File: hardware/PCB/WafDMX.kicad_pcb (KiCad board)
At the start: 2 copper layers, 91.4 x 101.6 mm, 54 parts, among them J1 Wuerth_7499010121A, J2 Screw_Terminal_01x02, J3 USB_B_Micro, J4 Conn_01x04_Female, Q1 MMDT2222A, U1 AMS1117-3.3, U2 LAN8720A, U3 CH340C, U4 ESP32-WROOM-32D, U5 MAX3485, X1 ASV-50MHz

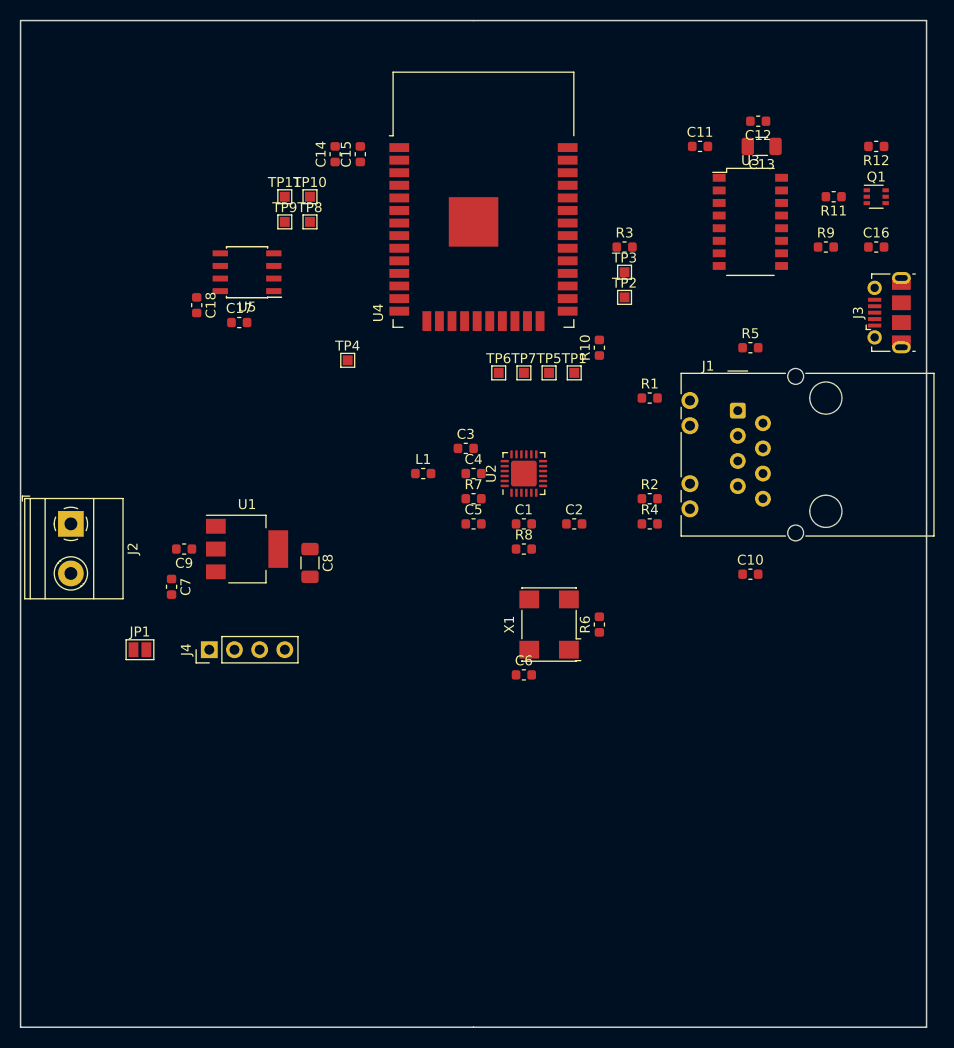
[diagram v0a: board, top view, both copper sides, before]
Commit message: Change Testpoints to TH, start placing
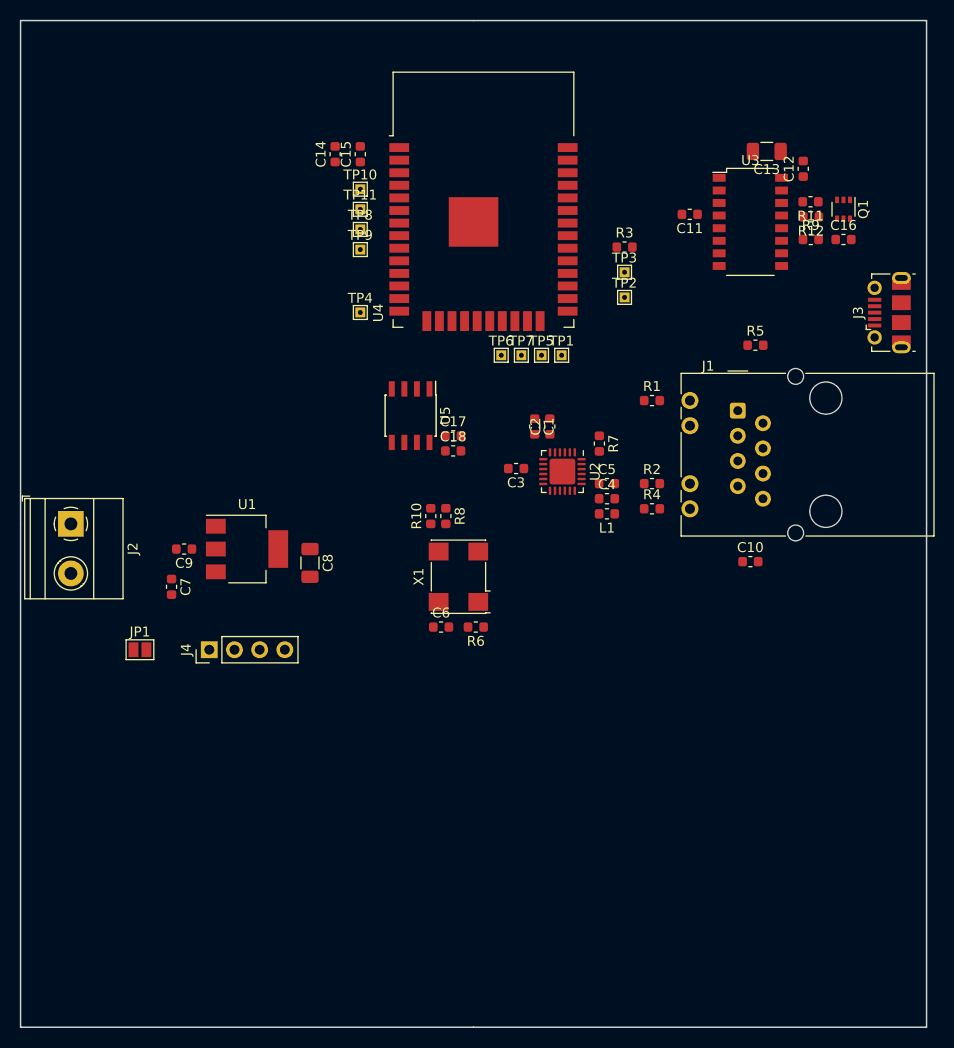
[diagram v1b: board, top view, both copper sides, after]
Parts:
- TP1, TP10, TP11, TP2, TP3, TP4, TP5, TP6, TP7, TP8, TP9: footprint TestPoint:TestPoint_Pad_1.0x1.0mm -> TestPoint:TestPoint_THTPad_1.0x1.0mm_Drill0.5mm
- moved C18 29.8 mm to (145.3, 94.2), turned to 0 degrees
- moved C17 24.4 mm to (145.3, 92.7)
- moved R10 24.0 mm to (143.0, 100.8)
- moved U5 22.0 mm to (141.0, 90.7), turned to 270 degrees
- moved L1 19.0 mm to (160.8, 100.6), turned to 180 degrees
- moved C5 14.1 mm to (160.8, 97.5)
- moved R7 13.9 mm to (160.0, 93.5), turned to 270 degrees
- moved C4 13.7 mm to (160.8, 99.1)
- moved R6 12.5 mm to (147.5, 112.0), turned to 180 degrees
- moved X1 10.3 mm to (145.8, 106.9)
- moved C2 10.1 mm to (155.0, 91.8), turned to 90 degrees
- moved C1 9.89 mm to (153.5, 91.8), turned to 270 degrees
- moved R12 9.69 mm to (181.4, 70.6)
- moved C6 9.65 mm to (144.0, 112.0)
- moved R8 8.55 mm to (144.5, 100.8), turned to 270 degrees
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
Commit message: First routing of PCB
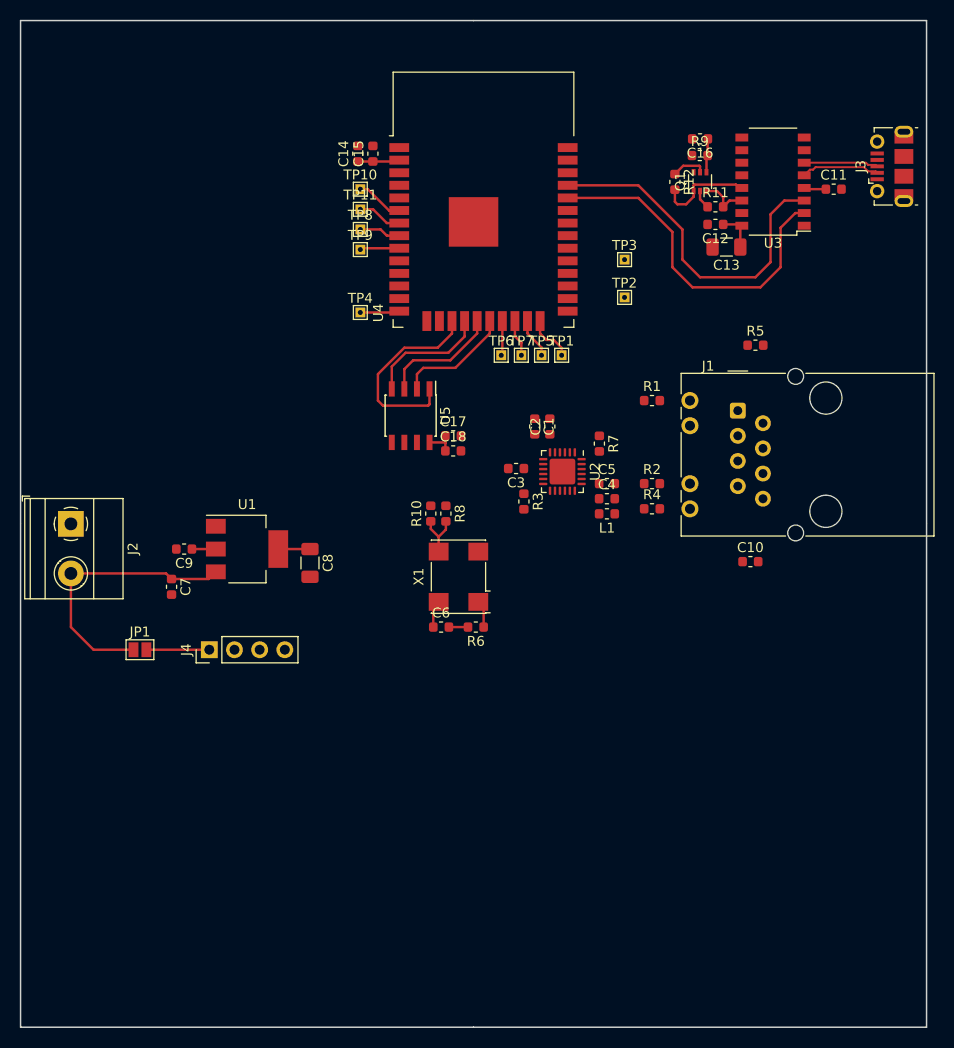
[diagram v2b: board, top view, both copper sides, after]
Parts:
- moved R3 27.6 mm to (152.4, 99.3), turned to 270 degrees
- moved C16 17.7 mm to (170.2, 62.7), turned to 180 degrees
- moved J3 14.8 mm to (189.5, 65.5)
- moved C11 14.7 mm to (183.7, 67.8), turned to 0 degrees
- moved Q1 14.7 mm to (170.2, 67.1), turned to 90 degrees
- moved R12 14.2 mm to (167.6, 67.1), turned to 270 degrees
- moved R9 14.0 mm to (170.2, 64.4)
- moved C12 10.5 mm to (171.7, 71.4), turned to 180 degrees
- moved C13 10.5 mm to (172.8, 73.7)
- moved R11 9.61 mm to (171.7, 69.6), turned to 0 degrees
- moved U3 4.66 mm to (177.5, 67.1), turned to 180 degrees
- moved C14 2.29 mm to (135.6, 64.2)
- moved C15 1.27 mm to (137.2, 64.2)
- moved TP3 1.27 mm to (162.6, 74.9)
- moved R10 0.25 mm to (143.0, 100.6)
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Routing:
- net /ESP32_TX: track 0.00 -> 35.5 mm
- net /ESP32_RX: track 0.00 -> 35.1 mm
- net VCC: track 0.00 -> 27.8 mm
- net /DMX_MAX_OUT: track 0.00 -> 20.1 mm
- net +3V3: track 0.00 -> 20.0 mm
- net /DMX_MAX_IN: track 0.00 -> 12.4 mm
- net /DMX_DE: track 0.00 -> 12.1 mm
- net /DMX_RE: track 0.00 -> 11.8 mm
- net /DTR: track 0.00 -> 9.72 mm
- net /USB_DN: track 0.00 -> 7.93 mm
- net /USB_DP: track 0.00 -> 7.51 mm
- net Net-(J4-Pad1): track 0.00 -> 6.35 mm
- net /PHY_CLK: track 0.00 -> 5.24 mm
- net /RTS: track 0.00 -> 5.05 mm
- net Net-(TP10-Pad1): track 0.00 -> 4.82 mm
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
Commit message: Add routing
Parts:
- added J5: XLR3, WafDMX:XLR_Neutrik_NC3FAAH_Horizontal, F.Cu at (117.5, 94.5)
- added J6: XLR3, WafDMX:XLR_Neutrik_NC3MAAH_Horizontal, F.Cu at (117.5, 120.6)
- J2: footprint TerminalBlock_Phoenix:TerminalBlock_Phoenix_MKDS-1,5-2_1x02_P5.00mm_Horizontal -> WafDMX:TerminalBlock_WAGO_2604-1102_2x05_P5.00mm_30Degree
- R3, R4: value 33R -> 10K
- moved J3 88.8 mm to (146.4, 143.2), turned to 0 degrees
- moved C11 75.3 mm to (143.4, 131.4), turned to 180 degrees
- moved U3 67.6 mm to (144.8, 126.2), turned to 90 degrees
- moved C13 59.1 mm to (138.2, 121.5), turned to 90 degrees
- moved R11 58.4 mm to (142.9, 120.4), turned to 270 degrees
- moved R12 58.3 mm to (145.9, 121.2), turned to 180 degrees
- moved C12 58.2 mm to (140.5, 120.4), turned to 90 degrees
- moved Q1 57.4 mm to (145.4, 118.9), turned to 0 degrees
- moved J1 55.8 mm to (121.8, 70.5), turned to 180 degrees
- moved C6 52.0 mm to (153.8, 61.0), turned to 180 degrees
- moved C16 51.9 mm to (130.3, 95.9), turned to 270 degrees
- moved C10 51.5 mm to (134.5, 73.9)
- moved R6 51.1 mm to (150.3, 61.0), turned to 0 degrees
- moved R2 49.0 mm to (130.5, 63.1), turned to 180 degrees
- moved R9 48.9 mm to (130.3, 92.7), turned to 270 degrees
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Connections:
- J3 pad 1: (no net) -> Net-(J3-Pad1)
- J3 pad 4: (no net) -> Net-(J3-Pad4)
- U2 pad 14: (no net) -> Net-(U2-Pad14)
- U2 pad 4: (no net) -> Net-(U2-Pad4)
- U3 pad 10: (no net) -> Net-(U3-Pad10)
- U3 pad 11: (no net) -> Net-(U3-Pad11)
- U3 pad 12: (no net) -> Net-(U3-Pad12)
- U3 pad 15: (no net) -> Net-(U3-Pad15)
- U3 pad 7: (no net) -> Net-(U3-Pad7)
- U3 pad 8: (no net) -> Net-(U3-Pad8)
- U3 pad 9: (no net) -> Net-(U3-Pad9)
- U4 pad 32: (no net) -> Net-(U4-Pad32)
- U4 pad 4: (no net) -> Net-(U4-Pad4)
- U4 pad 5: (no net) -> Net-(U4-Pad5)
- U5 pad 6: (no net) -> Net-(J5-Pad3)
- U5 pad 7: (no net) -> Net-(J5-Pad2)
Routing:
- net +3V3: track 20.0 -> 203.3 mm, vias 0 -> 10
- net Net-(J5-Pad3): track 0.00 -> 65.0 mm
- net /PHY_CLK_EN: track 2.76 -> 65.7 mm
- net /IO0: track 0.00 -> 62.8 mm
- net /PHY_POWER: track 0.00 -> 61.6 mm, vias 0 -> 2
- net /SMI_MDIO: track 0.00 -> 56.6 mm, vias 0 -> 2
- net /EMAC_TXD0: track 0.00 -> 54.9 mm
- net /EMAC_RX_DV: track 0.00 -> 54.4 mm, vias 0 -> 2
- net /PHY_TX_N: track 0.00 -> 53.8 mm
- net /EMAC_TX_EN: track 0.00 -> 52.5 mm
- net /EMAC_TXD1: track 0.00 -> 51.6 mm, vias 0 -> 2
- net /PHY_TX_P: track 0.00 -> 49.3 mm
- net /SPI_CLK: track 0.00 -> 48.4 mm
- net /EMAC_RXD1: track 0.00 -> 48.0 mm
- net /SPI_MOSI: track 0.00 -> 47.9 mm
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- added copper zone on B.Cu, net GND
- added copper zone on F.Cu, net GND
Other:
- board size 91.4 x 101.6 mm -> 61.8 x 90 mm

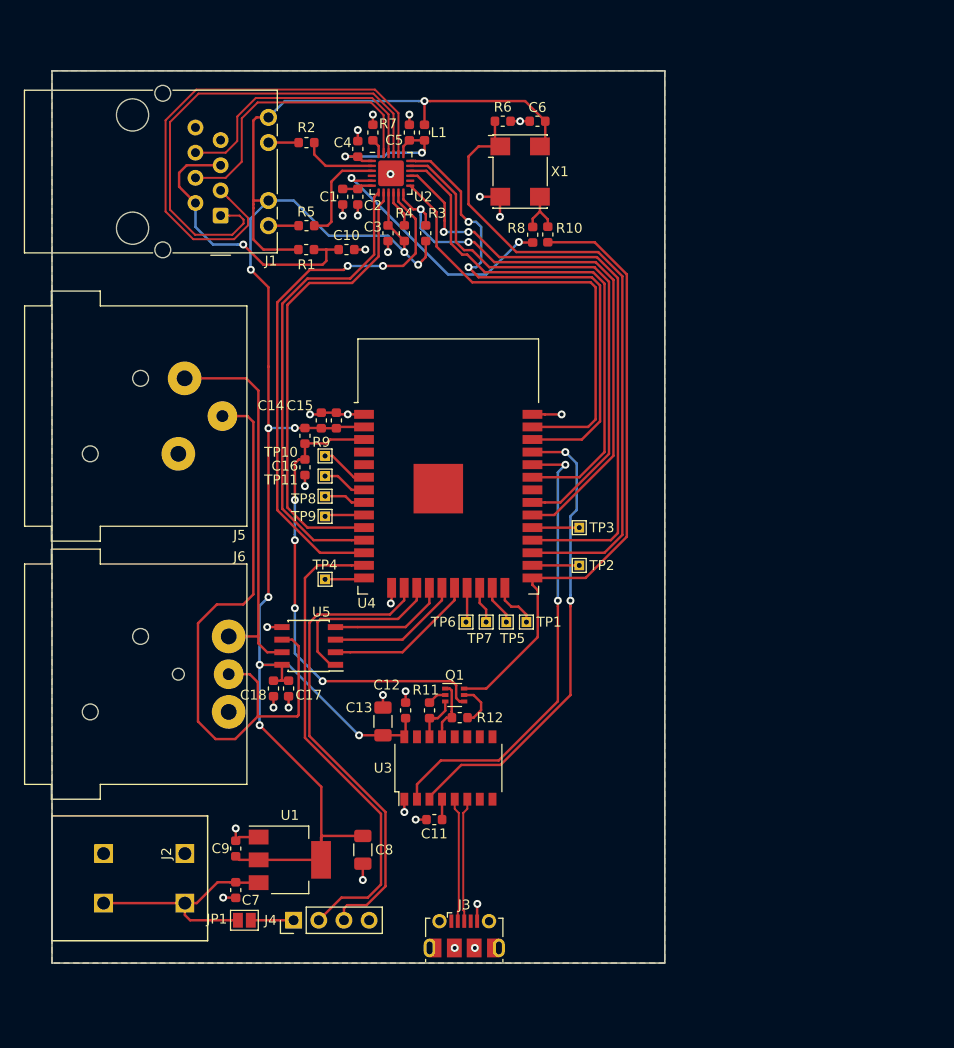
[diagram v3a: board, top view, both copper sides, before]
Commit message: Add 3V3-5V level shifter
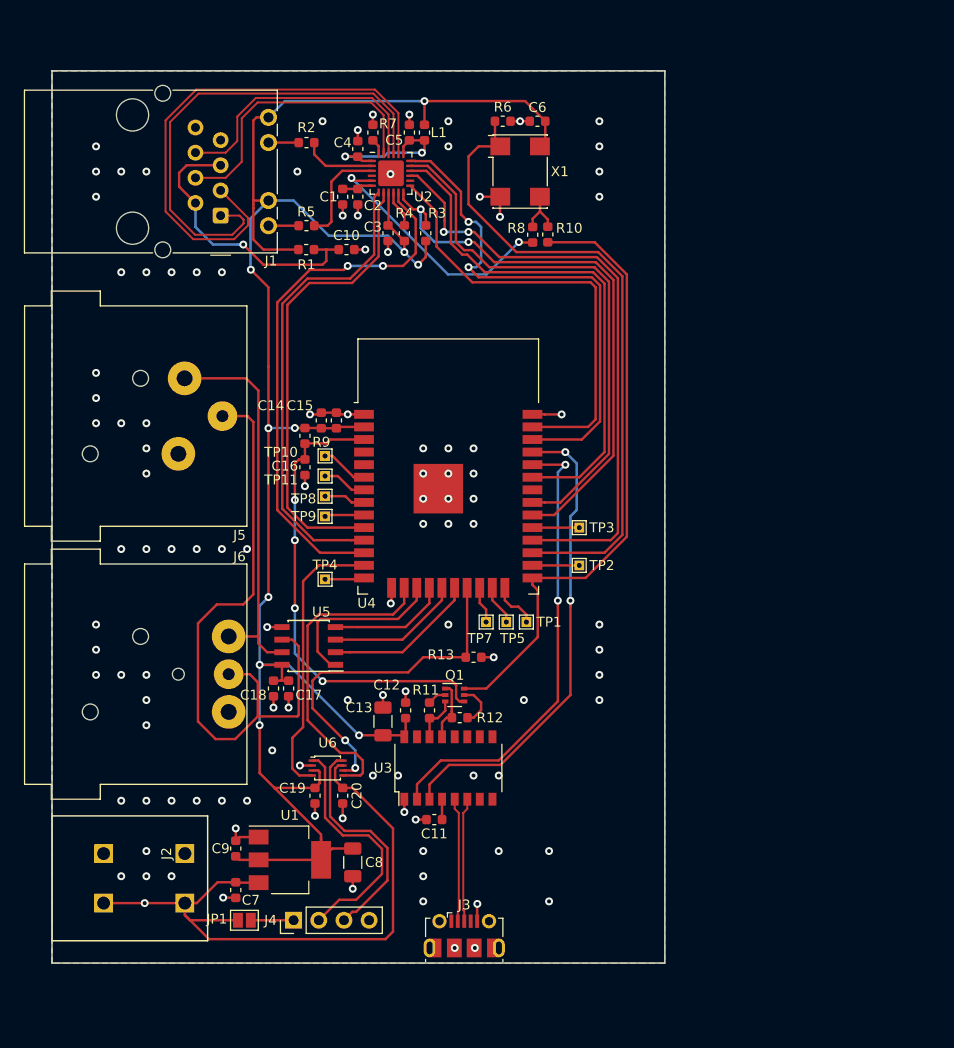
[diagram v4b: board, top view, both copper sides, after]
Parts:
- removed TP6: TestPoint, TestPoint:TestPoint_THTPad_1.0x1.0mm_Drill0.5mm
- added C19: 0.1 uF, Capacitor_SMD:C_0603_1608Metric, F.Cu at (131.3, 129.0)
- added C20: 0.1 uF, Capacitor_SMD:C_0603_1608Metric, F.Cu at (134.1, 129.0)
- added R13: R_Small, Resistor_SMD:R_0603_1608Metric, F.Cu at (147.3, 115.1)
- added U6: TXB0102DCU, Package_SO:VSSOP-8_2.4x2.1mm_P0.5mm, F.Cu at (132.6, 126.2)
- moved C8 1.63 mm to (135.1, 135.8)
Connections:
- J3 pad 1: Net-(J3-Pad1) -> (no net)
- J3 pad 4: Net-(J3-Pad4) -> (no net)
- J4 pad 2: /SPI_CLK -> /5V_SPI_CLK
- J4 pad 3: /SPI_MOSI -> /5V_SPI_MOSI
- U2 pad 14: Net-(U2-Pad14) -> (no net)
- U2 pad 4: Net-(U2-Pad4) -> (no net)
- U3 pad 10: Net-(U3-Pad10) -> (no net)
- U3 pad 11: Net-(U3-Pad11) -> (no net)
- U3 pad 12: Net-(U3-Pad12) -> (no net)
- U3 pad 15: Net-(U3-Pad15) -> (no net)
- U3 pad 7: Net-(U3-Pad7) -> (no net)
- U3 pad 8: Net-(U3-Pad8) -> (no net)
- U3 pad 9: Net-(U3-Pad9) -> (no net)
- U4 pad 21: Net-(TP6-Pad1) -> /SPI_OE
- U4 pad 32: Net-(U4-Pad32) -> (no net)
- U4 pad 4: Net-(U4-Pad4) -> (no net)
- U4 pad 5: Net-(U4-Pad5) -> (no net)
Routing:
- net VCC: track 23.3 -> 66.0 mm, vias 0 -> 1
- net /SPI_OE: track 0.00 -> 35.5 mm, vias 0 -> 2
- net /5V_SPI_CLK: track 0.00 -> 24.6 mm
- net /5V_SPI_MOSI: track 0.00 -> 23.0 mm
- net /SPI_CLK: track 48.4 -> 28.5 mm
- net /SPI_MOSI: track 47.9 -> 32.4 mm
- net +3V3: track 203.3 -> 209.4 mm
- net GND: track 41.9 -> 46.8 mm, vias 29 -> 107
- net Net-(TP6-Pad1): track 3.50 -> 0.00 mm
- net /ESP32_TX: track 47.3 -> 48.0 mm
- net (no net): vias 0 -> 4
